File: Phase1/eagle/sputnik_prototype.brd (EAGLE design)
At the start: 100 x 80 mm, 76 parts, among them U1 MEGA128-M, U2 MIC5219 3.3V, Y1 32MHz, Y2 8MHZ

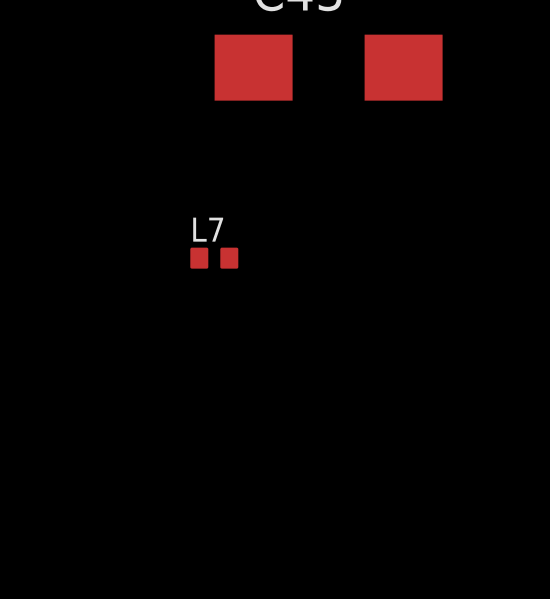
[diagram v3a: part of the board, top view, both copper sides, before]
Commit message: Updated schematic, added LDO datasheet
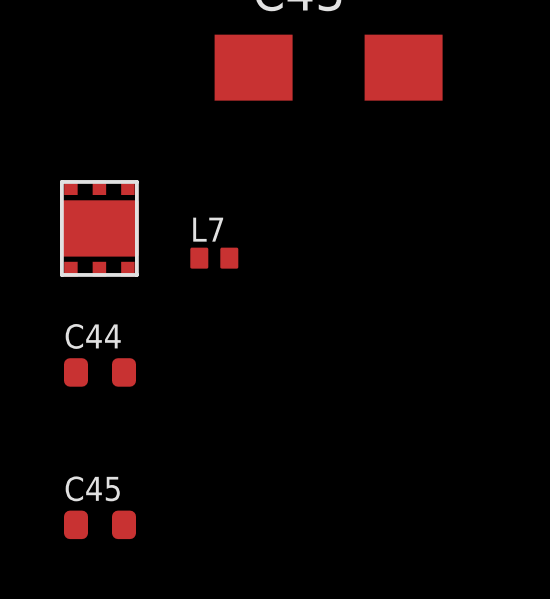
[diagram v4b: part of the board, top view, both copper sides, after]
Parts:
- added C44, C45: 10uF, rcl_custom:.0603-B-NOSILK
- added U$3: LD39200, psas_c3_team05:LD39200
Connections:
- new net N$26: C24.1, C43.+, L8.2, R1.2
- net GND: now also C44.1, C45.1, U$3.3
- net V+: now also C44.2, C45.2, U$3.1, U$3.2, U$3.5, U$3.6; no longer C24.1, C43.+, L8.2, R1.2
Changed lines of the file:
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@@
 <layers>
 <layer number="1" name="Top" color="4" fill="1" visible="yes" active="yes"/>
+<layer number="2" name="Route2" color="1" fill="3" visible="no" active="no"/>
+<layer number="3" name="Route3" color="4" fill="3" visible="no" active="no"/>
+<layer number="14" name="Route14" color="1" fill="6" visible="no" active="no"/>
+<layer number="15" name="Route15" color="4" fill="6" visible="no" active="no"/>
 <layer number="16" name="Bottom" color="1" fill="1" visible="yes" active="yes"/>
 <layer number="17" name="Pads" color="2" fill="1" visible="yes" active="yes"/>
@@
 <element name="C43" library="rcl" package="CT6032" value="" x="-53.34" y="-129.54"/>
 <element name="L7" library="rcl_custom" package=".0402-B-NOSILK" value="" x="-57.15" y="-135.89"/>
+<element name="U$3" library="psas_c3_team05" package="LD39200" value="LD39200" x="-62.23" y="-133.35"/>
+<element name="C44" library="rcl_custom" package=".0603-B-NOSILK" value="10uF" x="-60.96" y="-139.7"/>
+<element name="C45" library="rcl_custom" package=".0603-B-NOSILK" value="10uF" x="-60.96" y="-144.78"/>
 </elements>
 <signals>
@@
 <contactref element="C25" pad="2"/>
 <contactref element="C43" pad="-"/>
+<contactref element="U$3" pad="3"/>
+<contactref element="C44" pad="1"/>
+<contactref element="C45" pad="1"/>
+<wire x1="-61.76" y1="-139.7" x2="-61.76" y2="-144.78" width="0" layer="19" extent="1-1"/>
+<wire x1="-60.03" y1="-136.262" x2="-61.76" y2="-139.7" width="0" layer="19" extent="1-1"/>
+<wire x1="-50.84" y1="-129.54" x2="-60.03" y2="-136.262" width="0" layer="19" extent="1-1"/>
 <wire x1="-56.65" y1="-123.19" x2="-50.84" y2="-129.54" width="0" layer="19" extent="1-1"/>
 <wire x1="-56.65" y1="-119.38" x2="-56.65" y2="-123.19" width="0" layer="19" extent="1-1"/>
@@
 <signal name="V+">
 <contactref element="JP1" pad="1"/>
-<contactref element="C15" pad="2"/>
-<contactref element="C16" pad="2"/>
-<contactref element="U$6" pad="4"/>
-<contactref element="C17" pad="2"/>
-<contactref element="C18" pad="2"/>
-<contactref element="U$6" pad="10"/>
-<contactref element="C19" pad="2"/>
-<contactref element="C20" pad="2"/>
-<contactref element="U$6" pad="12"/>
-<contactref element="C21" pad="2"/>
-<contactref element="C22" pad="2"/>
-<contactref element="R1" pad="2"/>
-<contactref element="L8" pad="2"/>
 <contactref element="U$5" pad="10"/>
 <contactref element="C41" pad="2"/>
 <contactref element="U2" pad="1"/>
 <contactref element="U2" pad="3"/>
+<contactref element="U$3" pad="2"/>
+<contactref element="U$3" pad="1"/>
+<contactref element="U$6" pad="4"/>
+<contactref element="C15" pad="2"/>
+<contactref element="C16" pad="2"/>
+<contactref element="C18" pad="2"/>
+<contactref element="C17" pad="2"/>
+<contactref element="U$6" pad="10"/>
+<contactref element="C21" pad="2"/>
+<contactref element="C22" pad="2"/>
 <contactref element="U$6" pad="11"/>
-<contactref element="C24" pad="1"/>
-<contactref element="C43" pad="+"/>
-<wire x1="-57.65" y1="-119.38" x2="-55.84" y2="-129.54" width="0" layer="19" extent="1-1"/>
-<wire x1="-55.08" y1="-101.6" x2="-57.65" y2="-119.38" width="0" layer="19" extent="1-1"/>
+<contactref element="C20" pad="2"/>
+<contactref element="U$6" pad="12"/>
+<contactref element="C19" pad="2"/>
+<contactref element="U$3" pad="6"/>
+<contactref element="C44" pad="2"/>
+<contactref element="C45" pad="2"/>
+<contactref element="U$3" pad="5"/>
+<wire x1="-60.16" y1="-139.7" x2="-60.16" y2="-144.78" width="0" layer="19" extent="1-1"/>
+<wire x1="-60.98" y1="-136.262" x2="-60.16" y2="-139.7" width="0" layer="19" extent="1-1"/>
+<wire x1="-61.93" y1="-136.262" x2="-60.98" y2="-136.262" width="0" layer="19" extent="1-1"/>
+<wire x1="-61.93" y1="-133.535" x2="-61.93" y2="-136.262" width="0" layer="19" extent="1-1"/>
+<wire x1="-60.98" y1="-133.535" x2="-61.93" y2="-133.535" width="0" layer="19" extent="1-1"/>
+<wire x1="-55.08" y1="-101.6" x2="-60.98" y2="-133.535" width="0" layer="19" extent="1-1"/>
 <wire x1="-56.2" y1="-17.8101" x2="-55.08" y2="-101.6" width="0" layer="19" extent="1-1"/>
 <wire x1="-58.1" y1="-17.8101" x2="-56.2" y2="-17.8101" width="0" layer="19" extent="1-1"/>
@@
 <wire x1="-13.785" y1="41.89" x2="-17.78" y2="25.4" width="0" layer="19" extent="1-1"/>
 <wire x1="-14.44" y1="48.26" x2="-13.785" y2="41.89" width="0" layer="19" extent="1-1"/>
-<wire x1="-14.44" y1="52.07" x2="-14.44" y2="48.26" width="0" layer="19" extent="1-1"/>
-<wire x1="-18.25" y1="52.07" x2="-14.44" y2="52.07" width="0" layer="19" extent="1-1"/>
-<wire x1="-29.68" y1="44.45" x2="-18.25" y2="52.07" width="0" layer="19" extent="1-1"/>
+<wire x1="-29.68" y1="44.45" x2="-14.44" y2="48.26" width="0" layer="19" extent="1-1"/>
 <wire x1="-33.49" y1="44.45" x2="-29.68" y2="44.45" width="0" layer="19" extent="1-1"/>
 <wire x1="-37.3" y1="44.45" x2="-33.49" y2="44.45" width="0" layer="19" extent="1-1"/>
@@
 <wire x1="-56.65" y1="-115.57" x2="-56.65" y2="-135.89" width="0" layer="19" extent="1-1"/>
 </signal>
+<signal name="N$26">
+<contactref element="C24" pad="1"/>
+<contactref element="L8" pad="2"/>
+<contactref element="C43" pad="+"/>
+<contactref element="R1" pad="2"/>
+<wire x1="-57.65" y1="-119.38" x2="-55.84" y2="-129.54" width="0" layer="19" extent="1-1"/>
+<wire x1="-18.25" y1="52.07" x2="-57.65" y2="-119.38" width="0" layer="19" extent="1-1"/>
+<wire x1="-14.44" y1="52.07" x2="-18.25" y2="52.07" width="0" layer="19" extent="1-1"/>
+</signal>
 </signals>

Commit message: Fixed some stuff on schematic
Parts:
- removed C13: 100nF, rcl_custom:.0603-B-NOSILK
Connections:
- removed net N$4: C13.1, C25.1
- removed net PE4: U1.6
- removed net PE5: U1.7
- removed net PE6: U1.8
- net GND: no longer C25.2
- net N$20: now also C25.1; no longer C13.2
- net N$7: now also C25.2
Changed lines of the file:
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@@
 <element name="C11" library="rcl_custom" package=".0603-B-NOSILK" value="8.2pF" x="-15.24" y="44.45"/>
 <element name="C12" library="rcl_custom" package=".0603-B-NOSILK" value="8.2pF" x="-19.05" y="44.45"/>
-<element name="C13" library="rcl_custom" package=".0603-B-NOSILK" value="100nF" x="-22.86" y="44.45"/>
 <element name="C14" library="rcl_custom" package=".0603-B-NOSILK" value="100nF" x="-26.67" y="44.45"/>
 <element name="C15" library="rcl_custom" package=".0603-B-NOSILK" value="10uF" x="-30.48" y="44.45"/>
@@
 <contactref element="U$5" pad="6"/>
 <contactref element="C24" pad="2"/>
-<contactref element="C25" pad="2"/>
 <contactref element="C43" pad="-"/>
 <contactref element="U$3" pad="3"/>
@@
 <wire x1="-60.03" y1="-136.262" x2="-61.76" y2="-139.7" width="0" layer="19" extent="1-1"/>
 <wire x1="-50.84" y1="-129.54" x2="-60.03" y2="-136.262" width="0" layer="19" extent="1-1"/>
-<wire x1="-56.65" y1="-123.19" x2="-50.84" y2="-129.54" width="0" layer="19" extent="1-1"/>
-<wire x1="-56.65" y1="-119.38" x2="-56.65" y2="-123.19" width="0" layer="19" extent="1-1"/>
+<wire x1="-56.65" y1="-119.38" x2="-50.84" y2="-129.54" width="0" layer="19" extent="1-1"/>
 <wire x1="-56.68" y1="-106.68" x2="-56.65" y2="-119.38" width="0" layer="19" extent="1-1"/>
 <wire x1="-56.68" y1="-101.6" x2="-56.68" y2="-106.68" width="0" layer="19" extent="1-1"/>
@@
 <contactref element="L6" pad="2"/>
 <contactref element="C12" pad="2"/>
-<contactref element="C13" pad="2"/>
-<wire x1="-22.06" y1="44.45" x2="-18.25" y2="44.45" width="0" layer="19" extent="1-1"/>
-<wire x1="-48.73" y1="48.26" x2="-22.06" y2="44.45" width="0" layer="19" extent="1-1"/>
+<contactref element="C25" pad="1"/>
+<wire x1="-48.73" y1="48.26" x2="-57.65" y2="-123.19" width="0" layer="19" extent="1-1"/>
+<wire x1="-18.25" y1="44.45" x2="-48.73" y2="48.26" width="0" layer="19" extent="1-1"/>
 </signal>
 <signal name="N$21">
@@
 <wire x1="-50.8" y1="-3.81" x2="-55.88" y2="-41.91" width="0" layer="19" extent="1-1"/>
 <wire x1="-20.2522" y1="8.37" x2="-50.8" y2="-3.81" width="0" layer="19" extent="1-1"/>
-</signal>
-<signal name="PE4">
-<contactref element="U1" pad="6"/>
-</signal>
-<signal name="PE5">
-<contactref element="U1" pad="7"/>
-</signal>
-<signal name="PE6">
-<contactref element="U1" pad="8"/>
 </signal>
 <signal name="3.3V">
@@
 <wire x1="-56.2" y1="-15.2099" x2="-55.08" y2="-106.68" width="0" layer="19" extent="1-1"/>
 </signal>
-<signal name="N$4">
-<contactref element="C13" pad="1"/>
-<contactref element="C25" pad="1"/>
-<wire x1="-23.66" y1="44.45" x2="-57.65" y2="-123.19" width="0" layer="19" extent="1-1"/>
-</signal>
 <signal name="N$5">
 <contactref element="U$5" pad="8"/>
@@
 <contactref element="L8" pad="1"/>
 <contactref element="U$4" pad="6"/>
-<wire x1="-23.51" y1="52.88" x2="-16.04" y2="52.07" width="0" layer="19" extent="1-1"/>
+<contactref element="C25" pad="2"/>
+<wire x1="-23.51" y1="52.88" x2="-56.65" y2="-123.19" width="0" layer="19" extent="1-1"/>
+<wire x1="-16.04" y1="52.07" x2="-23.51" y2="52.88" width="0" layer="19" extent="1-1"/>
 </signal>
 <signal name="N$25">
